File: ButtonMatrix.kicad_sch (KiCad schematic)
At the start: 54 parts, among them SW201 SW_DPST, SW202 SW_DPST, SW203 SW_DPST, SW204 SW_DPST, SW205 SW_DPST, SW206 SW_DPST, SW207 SW_DPST, SW208 SW_DPST, SW209 SW_DPST, SW210 SW_DPST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

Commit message: Move encoder into its own sheet. Replace with MPG/Encoder combo.
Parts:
- C201, C202, C203, C204, C205, C206, C207, C208, C209: footprint (none) -> Capacitor_SMD:C_0805_2012Metric_Pad1.18x1.45mm_HandSolder
- D201, D202, D203, D204, D205, D206, D207, D208, D209, D210, D211, D212, D213, D214, D215, D216, D217, D218, D219, D220, D221, D222, D223, D224: footprint (none) -> Diode_SMD:D_SOD-323_HandSoldering
- R201, R202, R203, R204, R205, R206, R207, R208: footprint (none) -> Resistor_SMD:R_0805_2012Metric_Pad1.20x1.40mm_HandSolder
- SW201, SW202, SW203, SW204, SW205, SW206, SW207, SW208, SW209, SW210, SW211, SW212: footprint (none) -> MarcoK:TACTILE_SWITCH_6MM_SMD_2
- U201: footprint (none) -> Package_DIP:DIP-16_W7.62mm_LongPads

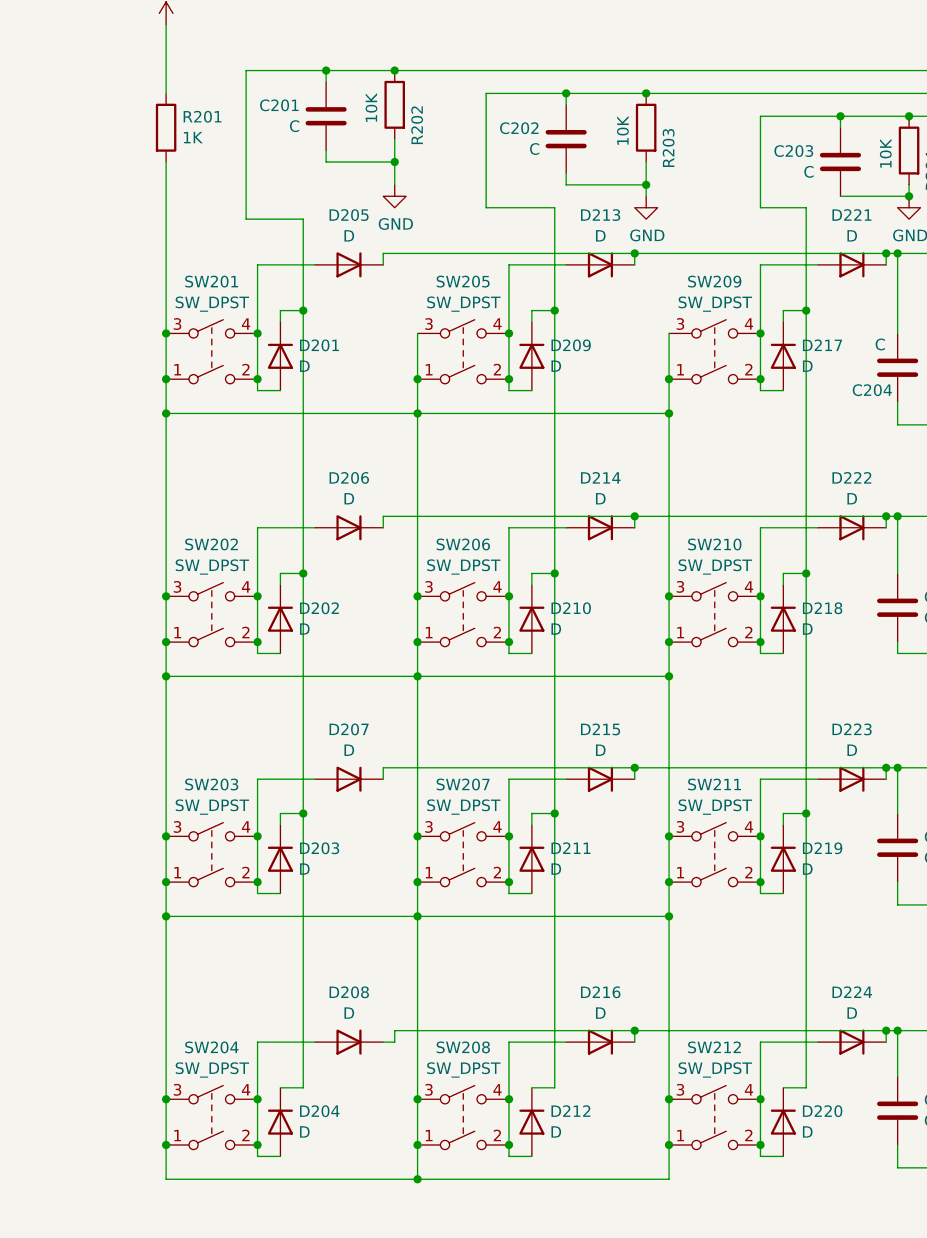
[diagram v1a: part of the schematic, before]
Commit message: Added the MPG. Switched tactile button model. Added JLC design rules.
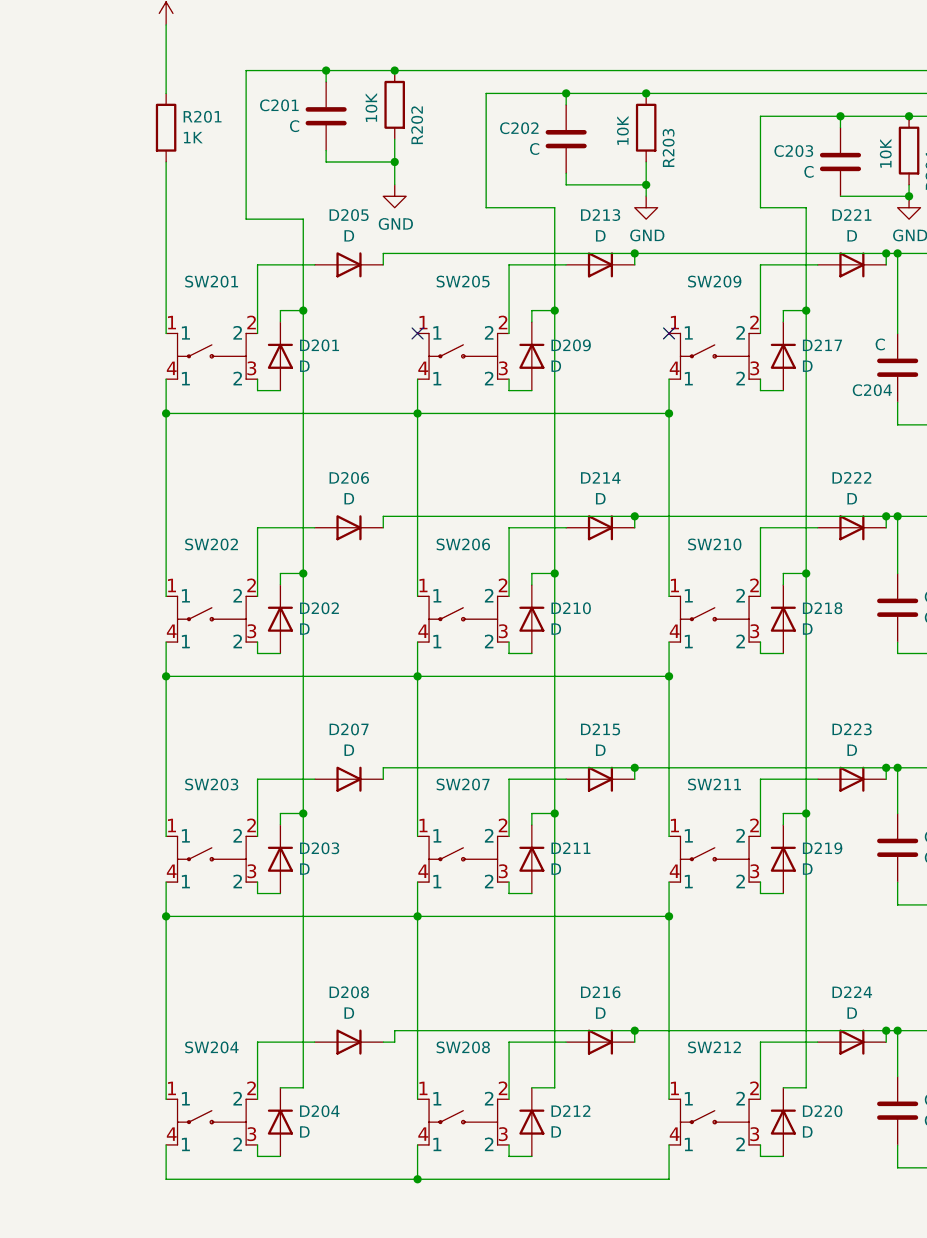
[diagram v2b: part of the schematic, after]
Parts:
- SW201, SW202, SW203, SW204, SW205, SW206, SW207, SW208, SW209, SW210, SW211, SW212: value SW_DPST -> FSM4JSMATR; footprint MarcoK:TACTILE_SWITCH_6MM_SMD_2 -> MarcoK:FSM4JSMATR; symbol Switch:SW_DPST -> MarcoK:FSM4JSMATR
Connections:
- net at D205.2 (A), SW201.2: no longer D201.2 (A), SW201.4
- net at D208.2 (A), SW204.2: no longer D204.2 (A), SW204.4
- net at D213.2 (A), SW205.2: no longer D209.2 (A), SW205.4
- net at D221.2 (A), SW209.2: no longer D217.2 (A), SW209.4
- net at D206.2 (A), SW202.2: no longer D202.2 (A), SW202.4
- net at D214.2 (A), SW206.2: no longer D210.2 (A), SW206.4
- net at D222.2 (A), SW210.2: no longer D218.2 (A), SW210.4
- net at D207.2 (A), SW203.2: no longer D203.2 (A), SW203.4
- net at D215.2 (A), SW207.2: no longer D211.2 (A), SW207.4
- net at D223.2 (A), SW211.2: no longer D219.2 (A), SW211.4
- net at D216.2 (A), SW208.2: no longer D212.2 (A), SW208.4
- net at D224.2 (A), SW212.2: no longer D220.2 (A), SW212.4
- new net: R201.2, SW201.1
- new net: D201.2 (A), SW201.3 (2)
- new net: SW201.4 (1), SW202.1, SW205.4 (1), SW206.1, SW209.4 (1), SW210.1
- new net: D204.2 (A), SW204.3 (2)
- new net: D209.2 (A), SW205.3 (2)
- new net: D217.2 (A), SW209.3 (2)
- new net: D202.2 (A), SW202.3 (2)
- new net: SW202.4 (1), SW203.1, SW206.4 (1), SW207.1, SW210.4 (1), SW211.1
- new net: D210.2 (A), SW206.3 (2)
- new net: D218.2 (A), SW210.3 (2)
- new net: D203.2 (A), SW203.3 (2)
- new net: SW203.4 (1), SW204.1, SW207.4 (1), SW208.1, SW211.4 (1), SW212.1
- new net: D211.2 (A), SW207.3 (2)
- new net: D219.2 (A), SW211.3 (2)
- new net: SW204.4 (1), SW208.4 (1), SW212.4 (1)
- new net: D212.2 (A), SW208.3 (2)
- new net: D220.2 (A), SW212.3 (2)
- now unconnected: SW205.1, SW209.1
- no-connect marks 1 -> 3
